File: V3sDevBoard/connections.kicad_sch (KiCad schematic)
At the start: 47 parts, among them J1 JST_ETHERNET, J2 USB_C_Receptacle_USB2.0_16P, J3 USB_C_Receptacle_USB2.0_16P, J4 Micro_SD_Card_Det1, J5 LCD, J6 MIPI CSI, J7 JST_I2C, U12 USBLC6-2SC6, U13 USBLC6-2SC6, U14 USBLC6-2SC6, U15 USBLC6-2SC6, U5 CH340C

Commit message: completing schematics
completing schematics, adding netclasses, fixing bugs, updating readme, starting pcb
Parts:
- added C16: 100n, Capacitor_SMD:C_0805_2012Metric_Pad1.18x1.45mm_HandSolder, symbol Device:C
- added J8: AudioJack, Connector_Audio:Jack_3.5mm_PJ320D_Horizontal, symbol Connector_Audio:AudioJack4
- added R58: 22R, Resistor_SMD:R_0805_2012Metric_Pad1.20x1.40mm_HandSolder, symbol Device:R
- added R69, R70: 4K7, Resistor_SMD:R_0805_2012Metric_Pad1.20x1.40mm_HandSolder, symbol Device:R
- added TP12: MIC, TestPoint:TestPoint_Pad_D1.0mm, symbol Connector:TestPoint
- added TP15: DTR, TestPoint:TestPoint_Pad_D1.0mm, symbol Connector:TestPoint
- added U16: USBLC6-2SC6, Package_TO_SOT_SMD:SOT-23-6, symbol Power_Protection:USBLC6-2SC6
- C17, C18: footprint (none) -> Capacitor_SMD:C_0805_2012Metric_Pad1.18x1.45mm_HandSolder
- R43: footprint (none) -> Resistor_SMD:R_0805_2012Metric_Pad1.20x1.40mm_HandSolder
- R46, R47: footprint Resistor_SMD:R_0805_2012Metric_Pad1.20x1.40mm_HandSolder -> Resistor_SMD:R_1206_3216Metric
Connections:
- net EPHY-RXP+ is gone; now on net EPHY-RX+: U14.3 (I/O2)
- net +3.3V: now also R69.1, R70.2
- net EPHY-RX-: now also C11.1, U14.6 (I/O1)
- net EPHY-TX+: now also C14.1, U15.4 (I/O2)
- net EPHY-TX-: now also C13.1, U15.6 (I/O1)
- net GND: now also C16.2, U16.2 (GND)
- net TWI0_SCK: now also U16.3 (I/O2), U16.4 (I/O2)
- net TWI0_SDA: now also U16.1 (I/O1), U16.6 (I/O1)
- net at J7.1 (Pin_1), R43.2: now also U16.5 (VBUS)
- net EPHY-RX+: now reaches C12.1, U14.4 (I/O2)
- net at U5.13 (~{DTR}): now also TP15.1
- net SCL0 renamed CSI_SCK
- net CSI_SCK: now also R69.2
- net SDA0 renamed CSI_SDA
- net CSI_SDA: now also R70.1
- new net: J8.S, TP12.1
- new net: C16.1, R58.2
- new net HPCOM: J8.R2, R58.1
- new net HPOUTL: J8.T
- new net HPOUTR: J8.R1
- no-connect marks 20 -> 19
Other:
- note added: "Audio"
- note added: "Ethernet"
- note added: "IMX708 0x1A i2c"
- note added: "USB otg"
- note removed: "Ethernet, optional"
- note removed: "USB for FEL-Mode"
- company: J.K. -> jakub.kmiecik@protonmail.com
- moved on the sheet: C15, C18, C44, D10, D11, J2, J5, J6, J7, R12, R13, R47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

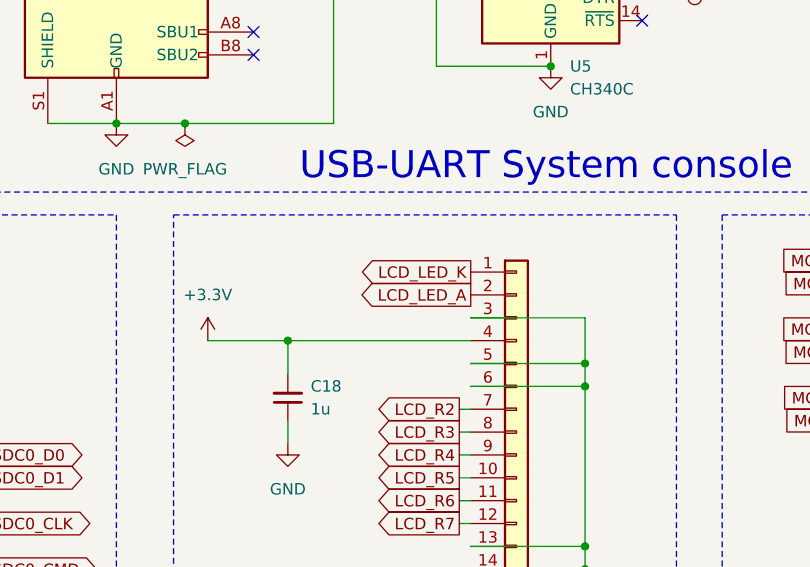
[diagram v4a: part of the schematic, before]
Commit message: first attempts to arrange components on a PCB
plus making footprints bme280&mpu6050 easier to hand solder.
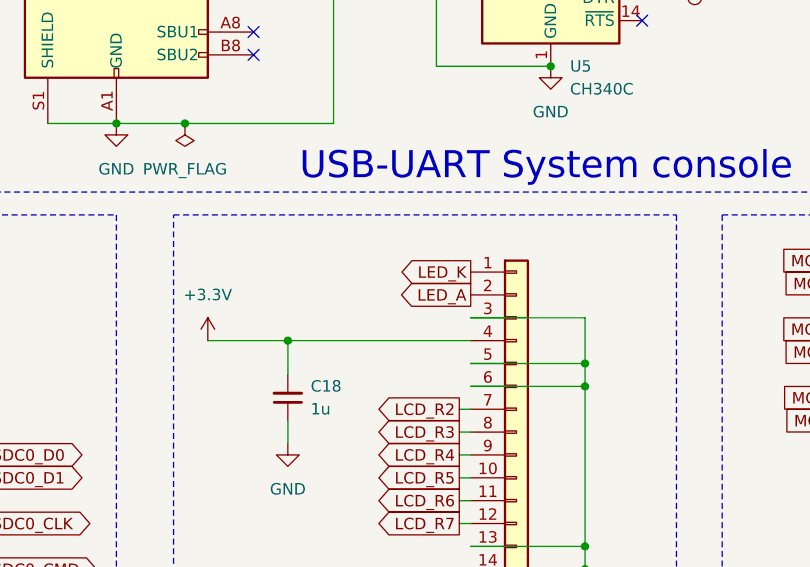
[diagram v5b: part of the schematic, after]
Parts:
- C43, C44: footprint Capacitor_SMD:C_0201_0603Metric_Pad0.64x0.40mm_HandSolder -> Capacitor_SMD:C_0603_1608Metric_Pad1.08x0.95mm_HandSolder
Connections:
- net LCD_LED_A renamed LED_A
- net LCD_LED_K renamed LED_K
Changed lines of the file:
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@@
 		)
 	)
-	(global_label "LCD_LED_A"
+	(global_label "LED_A"
 		(shape output)
 		(at 146.05 87.63 180)
@@
 		)
 		(property "Intersheetrefs" "${INTERSHEET_REFS}"
-			(at 133.0258 87.63 0)
+			(at 137.5615 87.63 0)
 			(effects
 				(font
@@
 		)
 	)
-	(global_label "LCD_LED_K"
+	(global_label "LED_K"
 		(shape output)
 		(at 146.05 85.09 180)
@@
 		)
 		(property "Intersheetrefs" "${INTERSHEET_REFS}"
-			(at 132.8444 85.09 0)
+			(at 137.3801 85.09 0)
 			(effects
 				(font
@@
 			)
 		)
-		(property "Footprint" "Capacitor_SMD:C_0201_0603Metric_Pad0.64x0.40mm_HandSolder"
+		(property "Footprint" "Capacitor_SMD:C_0603_1608Metric_Pad1.08x0.95mm_HandSolder"
 			(at 125.73 24.13 0)
 			(effects
@@
 			)
 		)
-		(property "Footprint" "Capacitor_SMD:C_0201_0603Metric_Pad0.64x0.40mm_HandSolder"
+		(property "Footprint" "Capacitor_SMD:C_0603_1608Metric_Pad1.08x0.95mm_HandSolder"
 			(at 237.49 24.13 0)
 			(effects

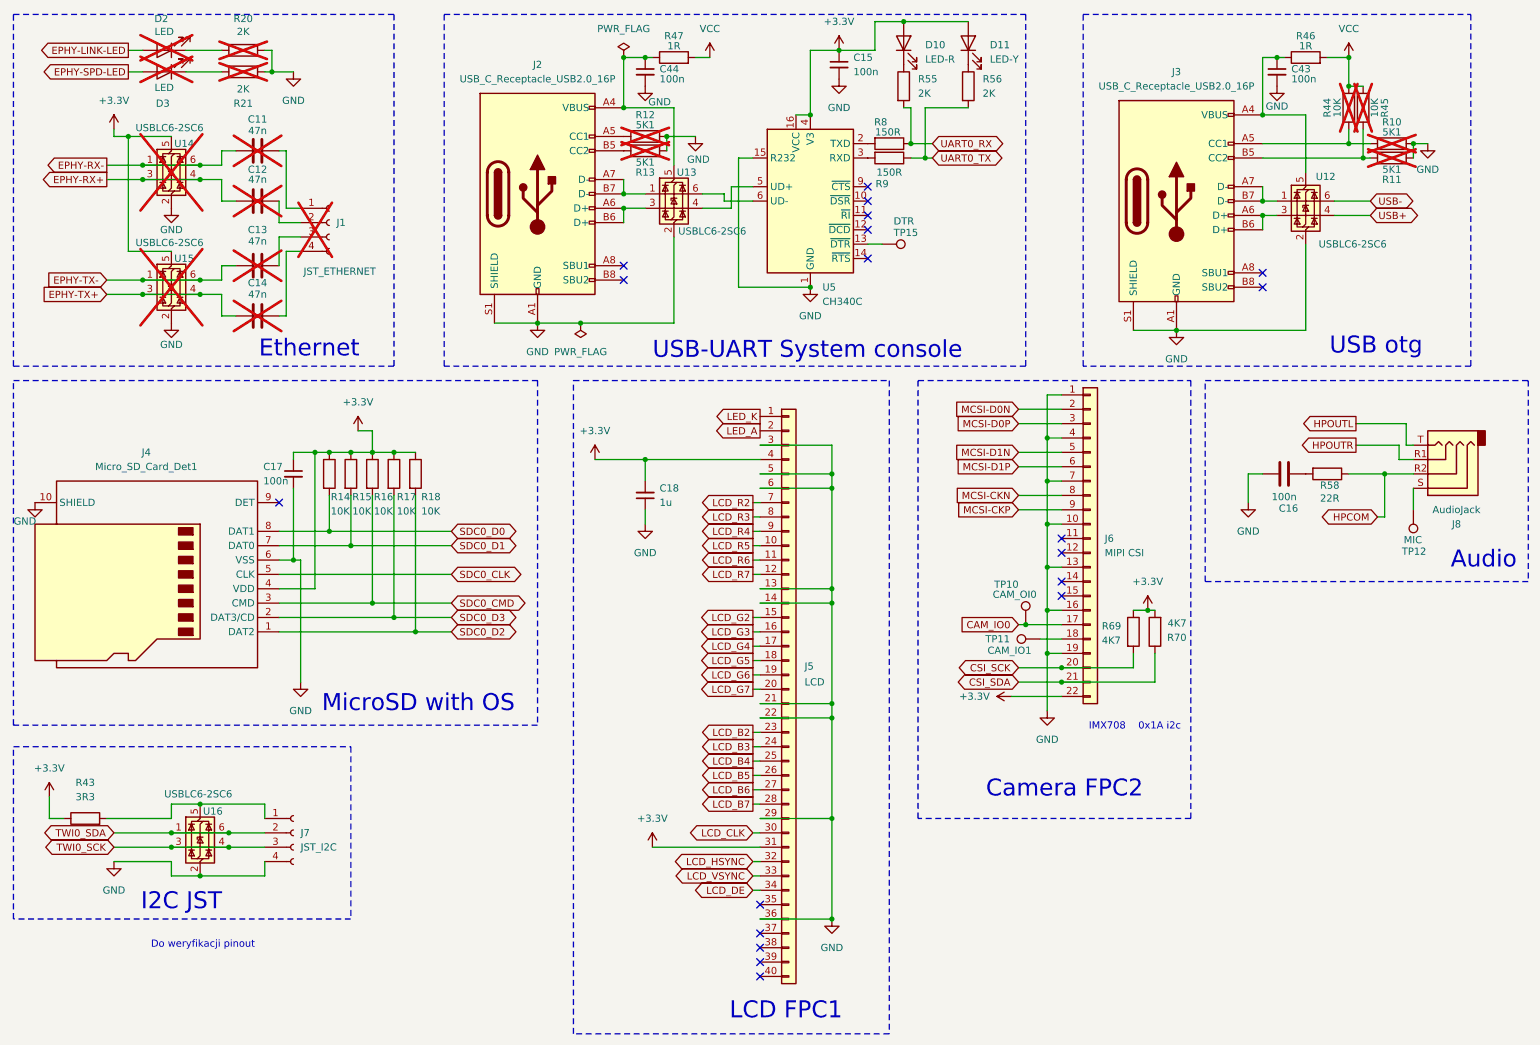
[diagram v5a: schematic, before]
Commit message: completing pcb desgin
Returning to project after month away. Switching to 4-layer desgin on 3313 stackup sig-gnd-pow-sig, changing size of some passive to 0603, connecting all components, adding silkscreen.
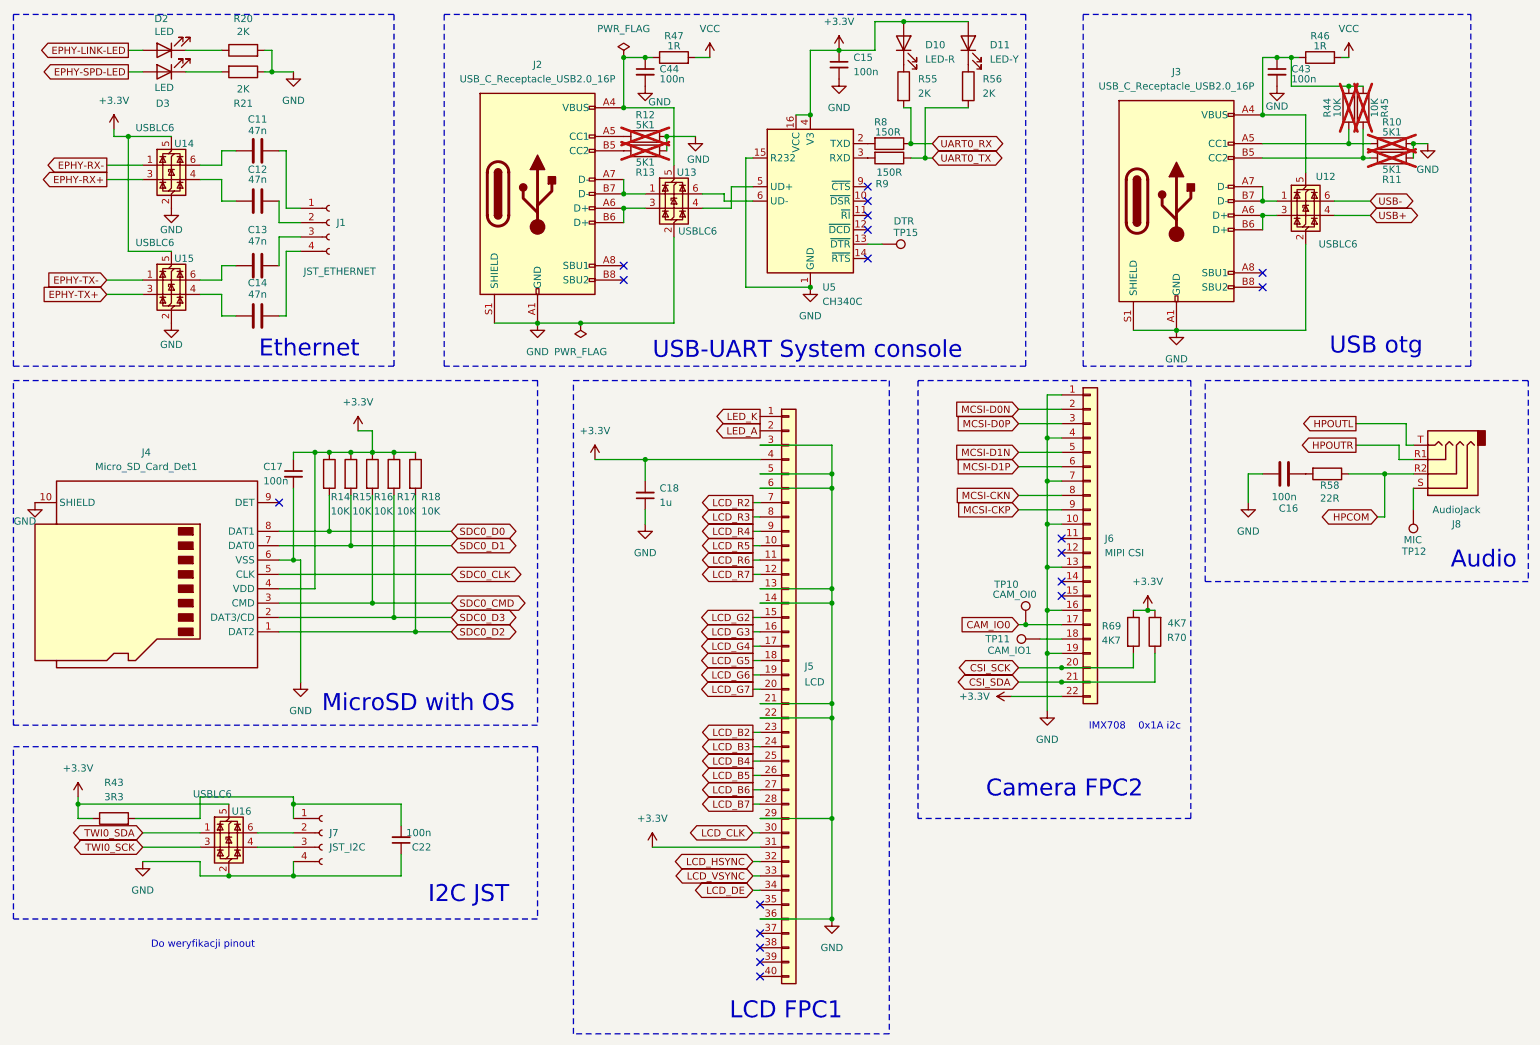
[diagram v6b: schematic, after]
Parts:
- added C22: 100n, Capacitor_SMD:C_0805_2012Metric_Pad1.18x1.45mm_HandSolder, symbol Device:C_Small
- C11, C12, C13, C14, D2, D3, J1: now fitted
- R10, R11, R12, R13, R14, R15, R16, R17, R18, R44, R45, R55, R56, R58, R69, R70, R8, R9: footprint Resistor_SMD:R_0805_2012Metric_Pad1.20x1.40mm_HandSolder -> Resistor_SMD:R_0603_1608Metric_Pad0.98x0.95mm_HandSolder
- R20, R21: footprint Resistor_SMD:R_0805_2012Metric_Pad1.20x1.40mm_HandSolder -> Resistor_SMD:R_0603_1608Metric_Pad0.98x0.95mm_HandSolder; now fitted
- R46, R47: footprint Resistor_SMD:R_1206_3216Metric -> Resistor_SMD:R_0805_2012Metric
- U12, U13, U16: value USBLC6-2SC6 -> USBLC6
- U14, U15: value USBLC6-2SC6 -> USBLC6; now fitted
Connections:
- net +3.3V: now also U16.5 (VBUS)
- net EPHY-RX+: no longer C12.1, U14.4 (I/O2)
- net EPHY-RX-: no longer C11.1, U14.6 (I/O1)
- net EPHY-TX+: no longer C14.1, U15.4 (I/O2)
- net EPHY-TX-: no longer C13.1, U15.6 (I/O1)
- net GND: now also C22.1
- net TWI0_SCK: no longer J7.3 (Pin_3), U16.4 (I/O2)
- net TWI0_SDA: no longer J7.2 (Pin_2), U16.6 (I/O1)
- net VCC: no longer R44.2, R45.1
- net at J7.1 (Pin_1), R43.2: now also C22.2; no longer U16.5 (VBUS)
- net at C43.1, J3.A4 (VBUS), J3.A9 (VBUS)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: now also R44.2, R45.1
- new net: C11.1, U14.6 (I/O1)
- new net: C14.1, U15.4 (I/O2)
- new net: J7.3 (Pin_3), U16.4 (I/O2)
- new net: J7.2 (Pin_2), U16.6 (I/O1)
- new net: C13.1, U15.6 (I/O1)
- new net: C12.1, U14.4 (I/O2)
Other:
- moved on the sheet: J7, R43, R46, U16

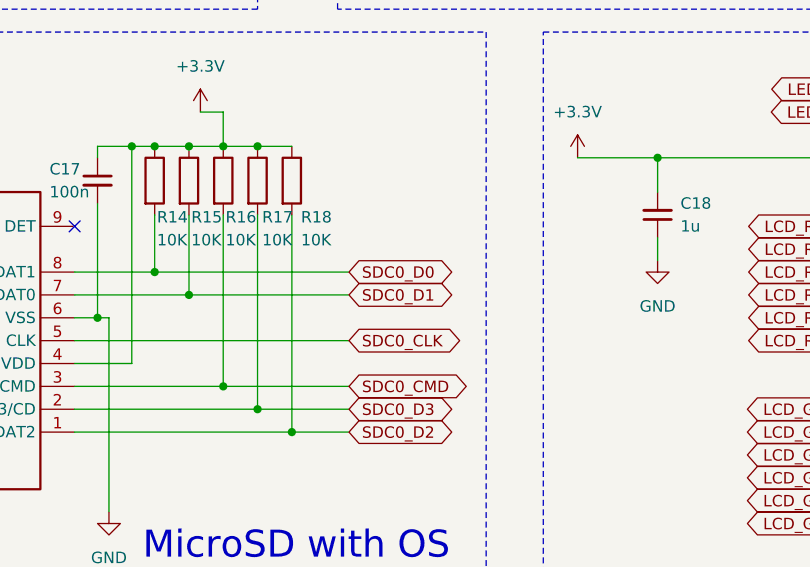
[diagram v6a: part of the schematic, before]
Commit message: fixing errors in revA
Fixing:
- Ther was mistake in SDIO for SDCard. Swaped data lines.
- RTC didn't have power without battery.
Updating readme.
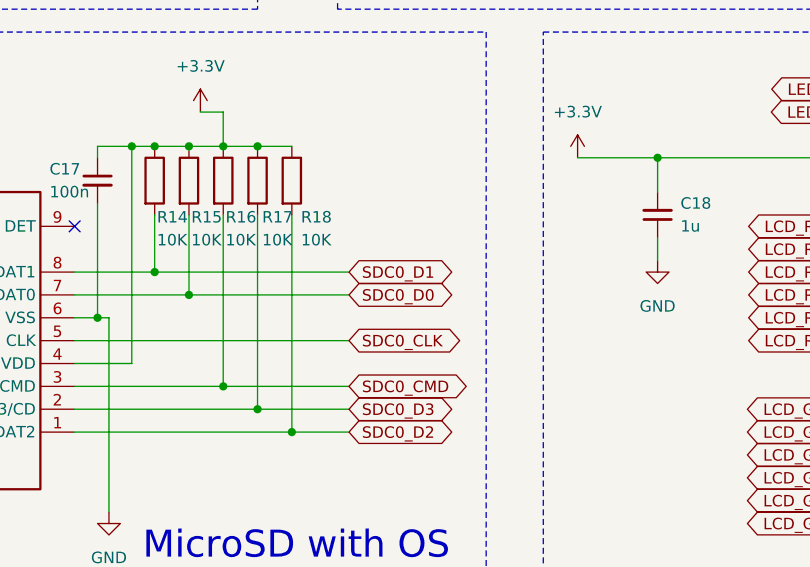
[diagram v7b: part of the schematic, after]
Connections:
- net SDC0_D0: now also J4.7 (DAT0), R15.2; no longer J4.8 (DAT1), R14.2
- net SDC0_D1: now also J4.8 (DAT1), R14.2; no longer J4.7 (DAT0), R15.2
